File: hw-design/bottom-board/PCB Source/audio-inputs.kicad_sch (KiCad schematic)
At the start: 83 parts, among them J7 NYS215, J8 NYS215, Q10 J110, Q11 J110, Q12 2N7002, Q13 2N7002, Q14 J110, Q15 J110, Q16 2N7002, Q9 2N7002, U8 LM4562

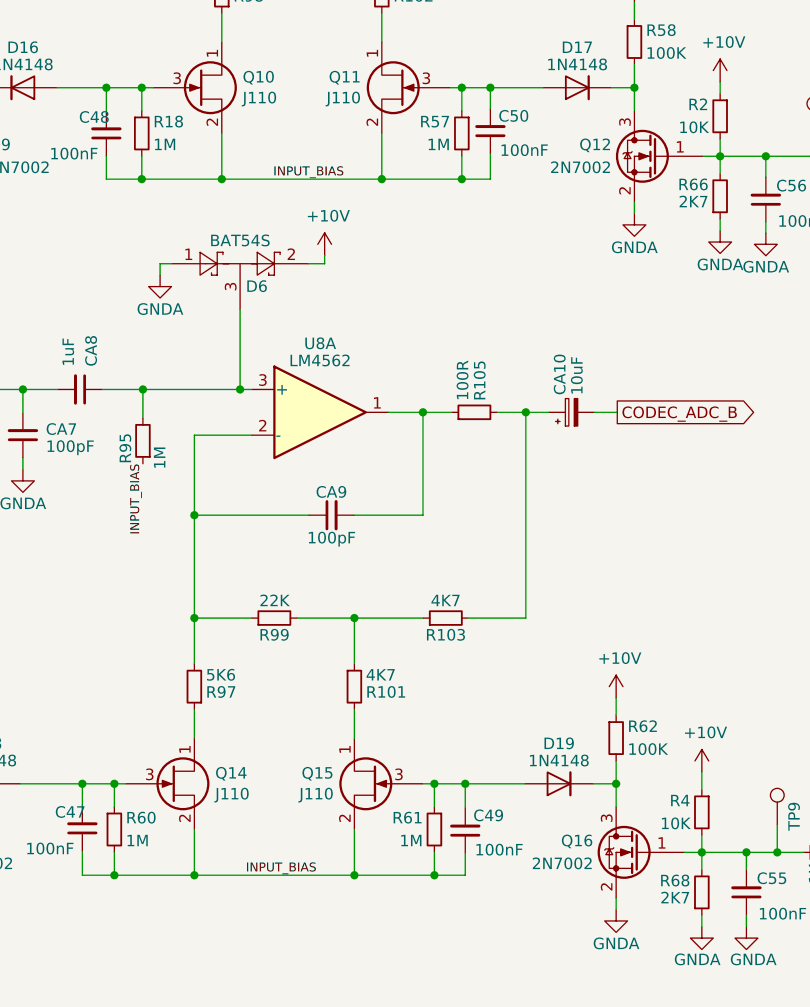
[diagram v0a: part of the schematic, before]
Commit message: separate input bias per channel (reduces crosstalk)
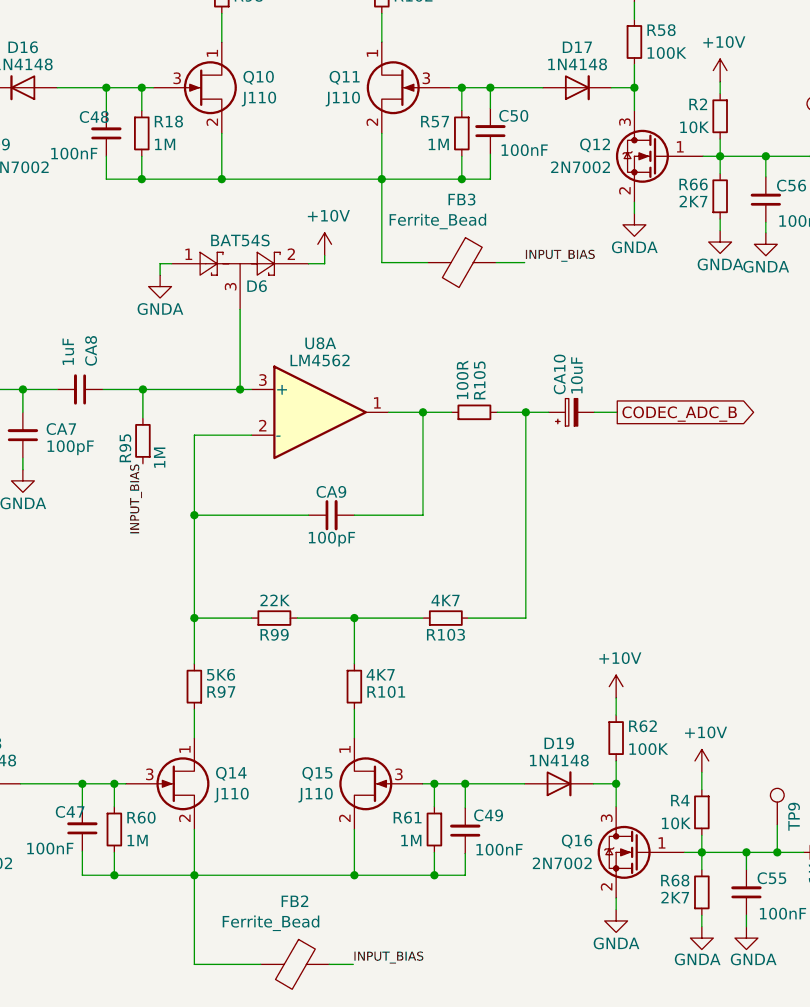
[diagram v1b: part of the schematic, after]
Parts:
- added FB2, FB3: Ferrite_Bead, Resistor_SMD:R_0603_1608Metric, symbol Device:Ferrite_Bead
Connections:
- net INPUT_BIAS: now also FB2.1, FB3.1; no longer C47.1, C48.1, C49.1, C50.1, Q10.2 (S), Q11.2 (S), Q14.2 (S), Q15.2 (S), R18.2, R57.2, R60.2, R61.2
- new net: C48.1, C50.1, FB3.2, Q10.2 (S), Q11.2 (S), R18.2, R57.2
- new net: C47.1, C49.1, FB2.2, Q14.2 (S), Q15.2 (S), R60.2, R61.2
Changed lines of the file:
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@@
   (no_connect (at 53.213 37.211))
   (no_connect (at 39.497 114.554))
+  (wire (pts (xy 115.443 97.917) (xy 115.443 88.646))
+    (stroke (width 0) (type default) (color 0 0 0 0))
+  )
   (wire (pts (xy 97.663 88.646) (xy 115.443 88.646))
     (stroke (width 0) (type default) (color 0 0 0 0))
@@
     (stroke (width 0) (type default) (color 0 0 0 0))
   )
+  (wire (pts (xy 120.523 97.917) (xy 115.443 97.917))
+    (stroke (width 0) (type default) (color 0 0 0 0))
+  )
   (wire (pts (xy 50.165 163.449) (xy 55.626 163.449))
     (stroke (width 0) (type default) (color 0 0 0 0))
@@
     (stroke (width 0) (type default) (color 0 0 0 0))
   )
-  (wire (pts (xy 94.615 165.989) (xy 94.615 160.909))
+  (wire (pts (xy 94.615 160.909) (xy 94.615 165.989))
     (stroke (width 0) (type default) (color 0 0 0 0))
   )
@@
     (stroke (width 0) (type default) (color 0 0 0 0))
   )
+  (wire (pts (xy 128.143 97.917) (xy 131.318 97.917))
+    (stroke (width 0) (type default) (color 0 0 0 0))
+  )
   (wire (pts (xy 47.371 119.634) (xy 47.371 131.191))
     (stroke (width 0) (type default) (color 0 0 0 0))
@@
     (stroke (width 0) (type default) (color 0 0 0 0))
   )
+  (wire (pts (xy 101.981 175.895) (xy 94.615 175.895))
+    (stroke (width 0) (type default) (color 0 0 0 0))
+  )
   (wire (pts (xy 52.451 55.88) (xy 52.451 56.642))
     (stroke (width 0) (type default) (color 0 0 0 0))
@@
     (stroke (width 0) (type default) (color 0 0 0 0))
   )
+  (wire (pts (xy 94.615 175.895) (xy 94.615 165.989))
+    (stroke (width 0) (type default) (color 0 0 0 0))
+  )
   (wire (pts (xy 102.743 34.671) (xy 104.013 34.671))
     (stroke (width 0) (type default) (color 0 0 0 0))
@@
     (stroke (width 0) (type default) (color 0 0 0 0))
   )
+  (wire (pts (xy 109.601 175.895) (xy 112.268 175.895))
+    (stroke (width 0) (type default) (color 0 0 0 0))
+  )
   (wire (pts (xy 40.386 109.474) (xy 39.497 109.474))
     (stroke (width 0) (type default) (color 0 0 0 0))
@@
     (effects (font (size 1.524 1.524)) (justify left bottom))
   )
-  (label "INPUT_BIAS" (at 100.33 165.989 0)
+  (label "INPUT_BIAS" (at 112.268 175.895 0)
     (effects (font (size 0.9906 0.9906)) (justify left bottom))
   )
@@
     (effects (font (size 0.9906 0.9906)) (justify left bottom))
   )
-  (label "INPUT_BIAS" (at 103.378 88.646 0)
+  (label "INPUT_BIAS" (at 131.318 97.917 0)
     (effects (font (size 0.9906 0.9906)) (justify left bottom))
   )
@@
     (pin "1")
   )
+  (symbol (lib_id "Device:Ferrite_Bead") (at 124.333 97.917 270) (unit 1)
+    (in_bom yes) (on_board yes)
+    (property "Reference" "FB3" (id 0) (at 124.333 90.9574 90))
+    (property "Value" "Ferrite_Bead" (id 1) (at 121.666 93.218 90))
+    (property "Footprint" "Resistor_SMD:R_0603_1608Metric" (id 2) (at 124.333 96.139 90)
+      (effects (font (size 1.27 1.27)) hide)
+    )
+    (property "Datasheet" "~" (id 3) (at 124.333 97.917 0)
+      (effects (font (size 1.27 1.27)) hide)
+    )
+    (property "MPN" "BLM18HD102SH1D" (id 4) (at 124.333 97.917 90)
+      (effects (font (size 1.27 1.27)) hide)
+    )
+    (pin "1")
+    (pin "2")
+  )
+  (symbol (lib_id "Device:Ferrite_Bead") (at 105.791 175.895 270) (unit 1)
+    (in_bom yes) (on_board yes)
+    (property "Reference" "FB2" (id 0) (at 105.791 168.9354 90))
+    (property "Value" "Ferrite_Bead" (id 1) (at 103.124 171.196 90))
+    (property "Footprint" "Resistor_SMD:R_0603_1608Metric" (id 2) (at 105.791 174.117 90)
+      (effects (font (size 1.27 1.27)) hide)
+    )
+    (property "Datasheet" "~" (id 3) (at 105.791 175.895 0)
+      (effects (font (size 1.27 1.27)) hide)
+    )
+    (property "MPN" "BLM18HD102SH1D" (id 4) (at 105.791 175.895 90)
+      (effects (font (size 1.27 1.27)) hide)
+    )
+    (pin "1")
+    (pin "2")
+  )
 )

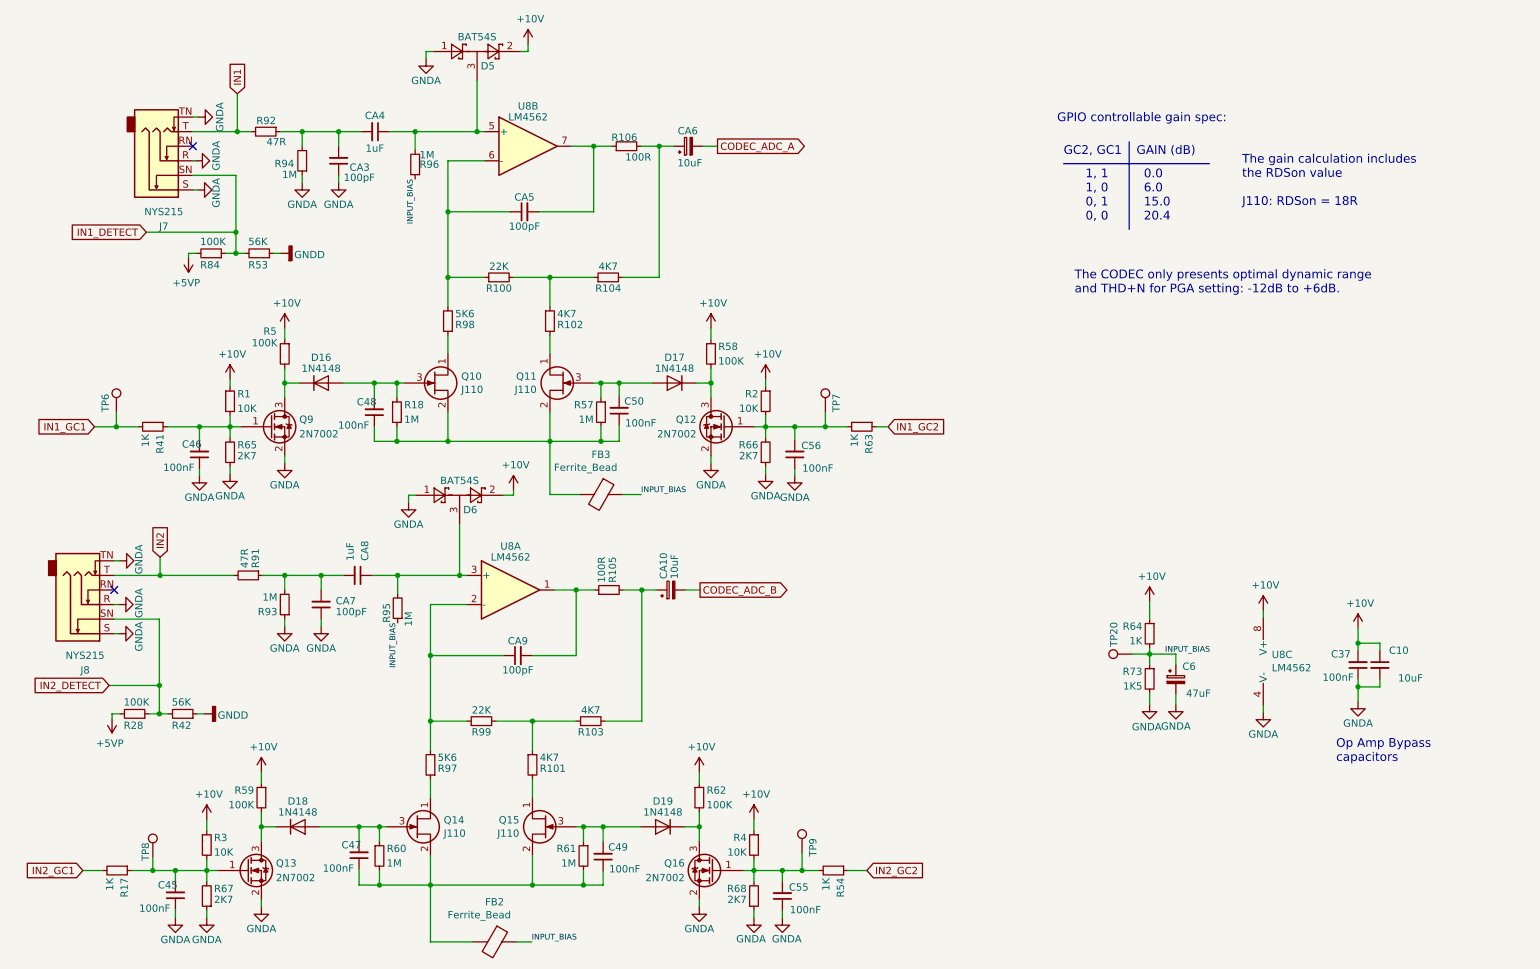
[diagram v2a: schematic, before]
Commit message: buffer bias per input
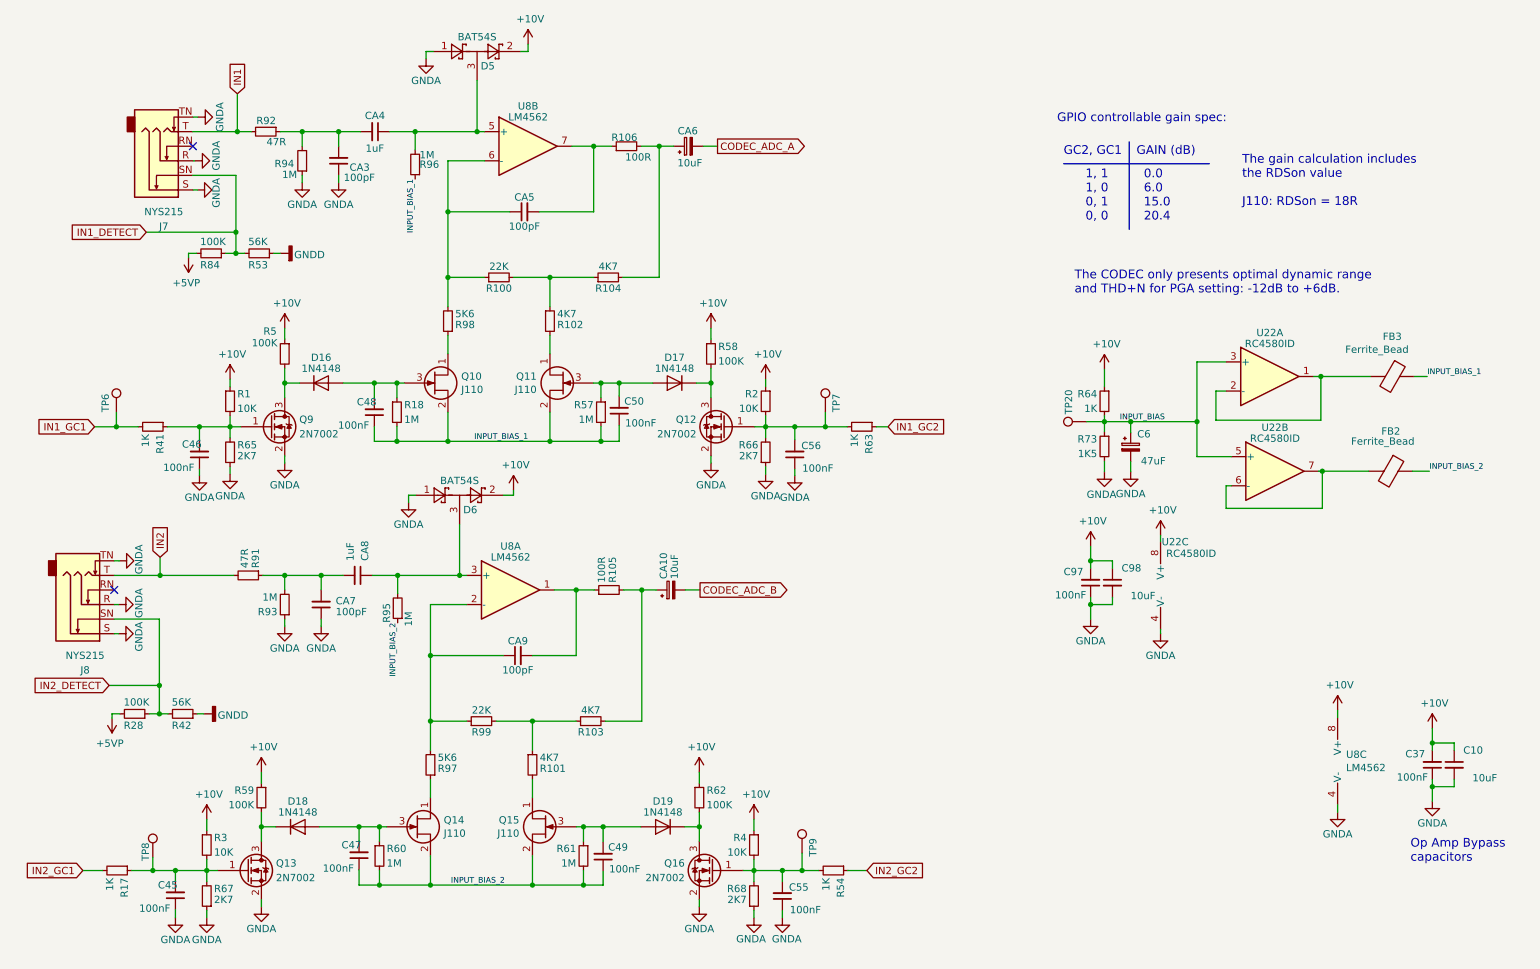
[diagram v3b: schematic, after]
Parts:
- added C97: 100nF, Capacitor_SMD:C_0603_1608Metric, symbol bottom-board-rescue:C_Small-Device
- added C98: 10uF, Capacitor_SMD:C_0805_2012Metric, symbol bottom-board-rescue:C_Small-Device
- added U22: RC4580ID, Package_SO:SOIC-8_3.9x4.9mm_P1.27mm, symbol bottom-board-rescue:LM4562-Amplifier_Operational
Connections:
- net +10V: now also C97.2, C98.1, U22.8 (V+)
- net GNDA: now also C97.1, C98.2, U22.4 (V-)
- net INPUT_BIAS: now also U22.3 (+), U22.5 (+); no longer FB2.1, FB3.1, R95.1, R96.1
- net INPUT_BIAS_1: now reaches C48.1, C50.1, Q10.2 (S), Q11.2 (S), R18.2, R57.2
- net INPUT_BIAS_1: now also FB3.1, R96.1; no longer FB3.2
- net INPUT_BIAS_2: now reaches C47.1, C49.1, Q14.2 (S), Q15.2 (S), R60.2, R61.2
- net INPUT_BIAS_2: now also FB2.1, R95.1; no longer FB2.2
- new net: FB2.2, U22.6 (-), U22.7
- new net: FB3.2, U22.1, U22.2 (-)
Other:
- moved on the sheet: C10, C37, C6, FB2, FB3, R64, R73, TP20, U8C

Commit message: update fabrication data
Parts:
- U22: value RC4580ID -> LM833DR2G; MPN OPA1678IDR -> LM833DR2G; MPN2 (none) -> OPA1678IDR
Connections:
- net at U22.6 (-), U22.7: now also FB3.2; no longer FB2.2
- net at U22.1, U22.2 (-): now also FB2.2; no longer FB3.2
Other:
- moved on the sheet: U22A, U22B
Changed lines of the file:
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@@
     (pin "1")
   )
-  (symbol (lib_id "bottom-board-rescue:LM4562-Amplifier_Operational") (at 241.808 93.853 0) (unit 2)
+  (symbol (lib_id "bottom-board-rescue:LM4562-Amplifier_Operational") (at 240.919 77.343 0) (unit 2)
     (in_bom yes) (on_board yes)
-    (property "Reference" "U22" (id 0) (at 241.808 86.233 0))
-    (property "Value" "RC4580ID" (id 1) (at 241.808 88.138 0))
-    (property "Footprint" "Package_SO:SOIC-8_3.9x4.9mm_P1.27mm" (id 2) (at 241.808 93.853 0)
+    (property "Reference" "U22" (id 0) (at 240.919 69.723 0))
+    (property "Value" "LM833DR2G" (id 1) (at 240.919 71.628 0))
+    (property "Footprint" "Package_SO:SOIC-8_3.9x4.9mm_P1.27mm" (id 2) (at 240.919 77.343 0)
       (effects (font (size 1.27 1.27)) hide)
     )
-    (property "Datasheet" "http://www.ti.com/lit/ds/symlink/opa1678.pdf" (id 3) (at 241.808 93.853 0)
+    (property "Datasheet" "http://www.ti.com/lit/ds/symlink/opa1678.pdf" (id 3) (at 240.919 77.343 0)
       (effects (font (size 1.27 1.27)) hide)
     )
-    (property "MPN" "OPA1678IDR" (id 4) (at 159.258 135.763 0)
+    (property "MPN" "LM833DR2G" (id 4) (at 158.369 119.253 0)
       (effects (font (size 1.27 1.27)) hide)
+    )
+    (property "MPN2" "OPA1678IDR" (id 5) (at 240.919 77.343 0)
+      (effects (font (size 1.524 1.524)) hide)
     )
     (pin "5")
@@
     (in_bom yes) (on_board yes)
     (property "Reference" "U22" (id 0) (at 224.409 106.172 0))
-    (property "Value" "RC4580ID" (id 1) (at 227.203 108.204 0))
+    (property "Value" "LM833DR2G" (id 1) (at 227.203 108.204 0))
     (property "Footprint" "Package_SO:SOIC-8_3.9x4.9mm_P1.27mm" (id 2) (at 224.409 113.792 0)
       (effects (font (size 1.27 1.27)) hide)
@@
       (effects (font (size 1.27 1.27)) hide)
     )
-    (property "MPN" "OPA1678IDR" (id 4) (at 141.859 155.702 0)
+    (property "MPN" "LM833DR2G" (id 4) (at 141.859 155.702 0)
       (effects (font (size 1.27 1.27)) hide)
+    )
+    (property "MPN2" "OPA1678IDR" (id 5) (at 224.409 113.792 0)
+      (effects (font (size 1.524 1.524)) hide)
     )
     (pin "4")
@@
     (pin "2")
   )
-  (symbol (lib_id "bottom-board-rescue:LM4562-Amplifier_Operational") (at 240.919 77.343 0) (unit 1)
+  (symbol (lib_id "bottom-board-rescue:LM4562-Amplifier_Operational") (at 241.808 93.853 0) (unit 1)
     (in_bom yes) (on_board yes)
-    (property "Reference" "U22" (id 0) (at 240.919 69.723 0))
-    (property "Value" "RC4580ID" (id 1) (at 240.919 71.628 0))
-    (property "Footprint" "Package_SO:SOIC-8_3.9x4.9mm_P1.27mm" (id 2) (at 240.919 77.343 0)
+    (property "Reference" "U22" (id 0) (at 241.808 86.233 0))
+    (property "Value" "LM833DR2G" (id 1) (at 241.808 88.138 0))
+    (property "Footprint" "Package_SO:SOIC-8_3.9x4.9mm_P1.27mm" (id 2) (at 241.808 93.853 0)
       (effects (font (size 1.27 1.27)) hide)
     )
-    (property "Datasheet" "http://www.ti.com/lit/ds/symlink/opa1678.pdf" (id 3) (at 240.919 77.343 0)
+    (property "Datasheet" "http://www.ti.com/lit/ds/symlink/opa1678.pdf" (id 3) (at 241.808 93.853 0)
       (effects (font (size 1.27 1.27)) hide)
     )
-    (property "MPN" "OPA1678IDR" (id 4) (at 158.369 119.253 0)
+    (property "MPN" "LM833DR2G" (id 4) (at 159.258 135.763 0)
       (effects (font (size 1.27 1.27)) hide)
     )
+    (property "MPN2" "OPA1678IDR" (id 5) (at 241.808 93.853 0)
+      (effects (font (size 1.524 1.524)) hide)
+    )
     (pin "1")
